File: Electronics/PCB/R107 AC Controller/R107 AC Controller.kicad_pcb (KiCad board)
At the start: 2 copper layers, 56 parts, among them J1 CAR POWER, J2 CONTROL, J3 ACCESSORY, J4 KNOB, J5 THERMOCOUPLE, J6 USB_B_Mini, J7 ISP, K1 G5LE-1, K2 G5LE-1, Q1 MMBT2222ALT1G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

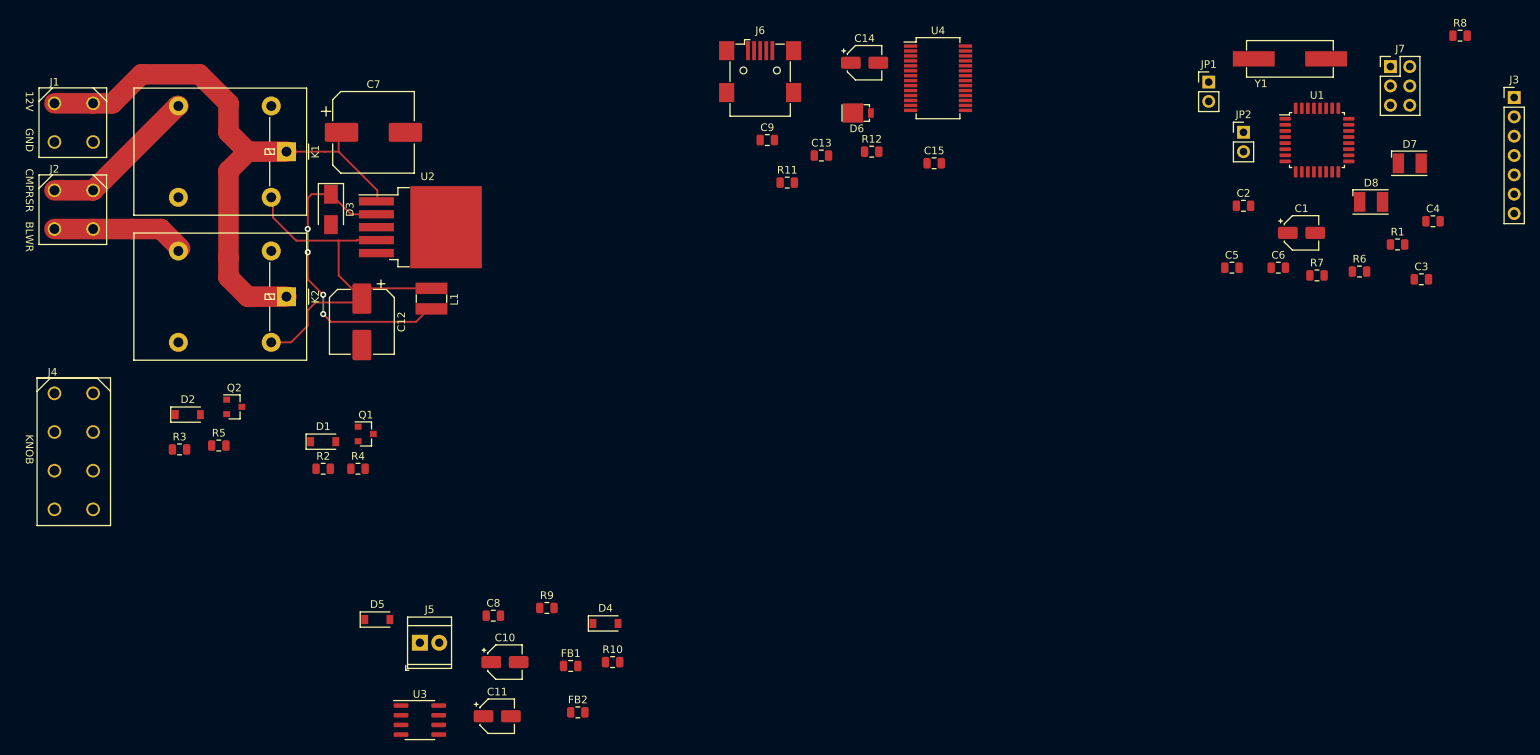
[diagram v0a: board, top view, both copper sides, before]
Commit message: Working on PCB. Added status LED and removed comms LEDs. Added jumper to reduce chances of noise on RX input keeping bootloader running.
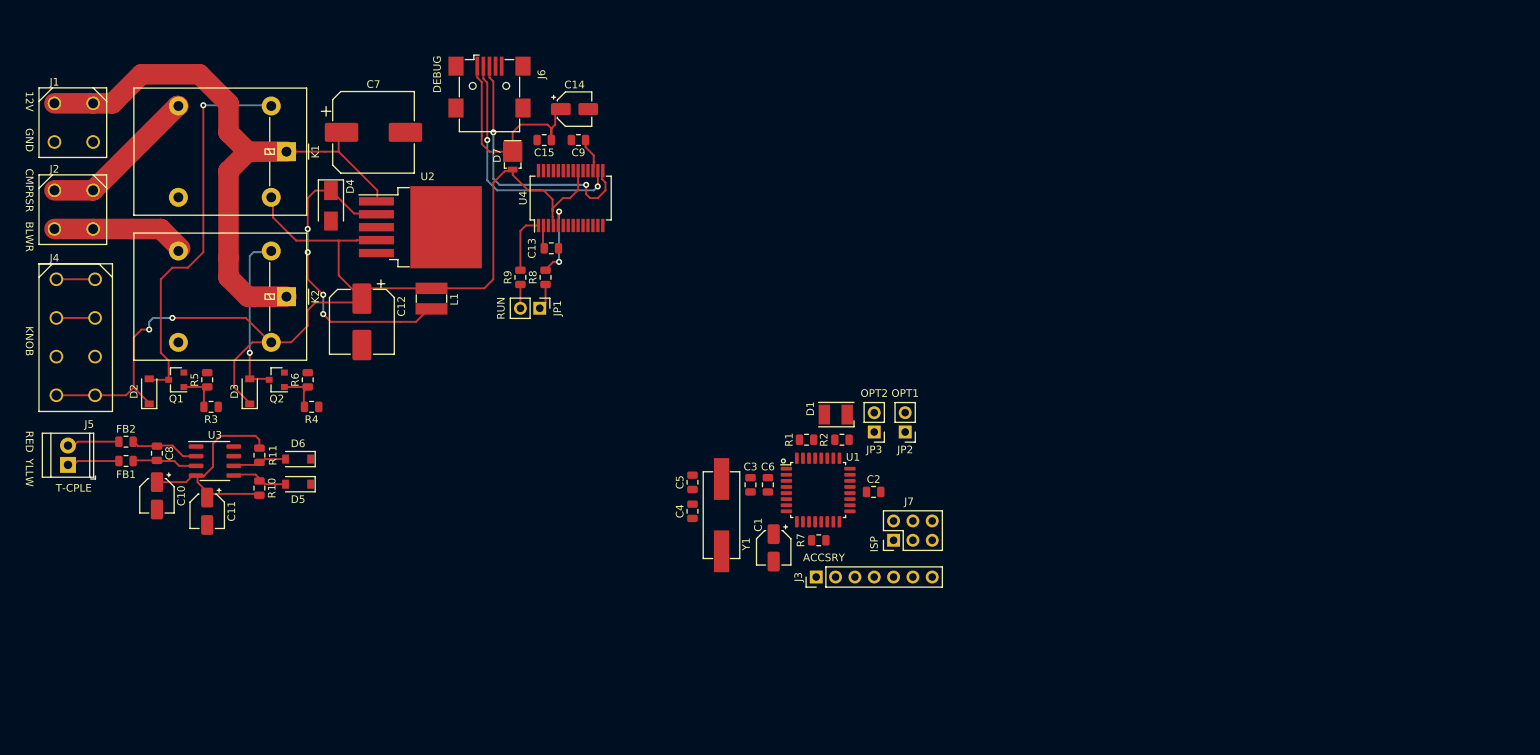
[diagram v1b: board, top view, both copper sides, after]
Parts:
- removed D8: GRN, LED_SMD:LED_PLCC-2
- removed R12: 1K, Resistor_SMD:R_0805_2012Metric
- added JP3: OPT2, Connector_PinHeader_2.54mm:PinHeader_1x02_P2.54mm_Vertical, F.Cu at (241.0, 69.8)
- D1: value MMSD4148T1G -> RED; footprint Diode_SMD:D_SOD-123 -> LED_SMD:LED_PLCC-2
- D3: value SK34ATR -> MMSD4148T1G; footprint Diode_SMD:D_SMA -> Diode_SMD:D_SOD-123
- D4: value MMSD4148T1G -> SK34ATR; footprint Diode_SMD:D_SOD-123 -> Diode_SMD:D_SMA
- D6: value SS1P3L-M3/84A -> MMSD4148T1G; footprint Britishideas:SMP_DO-220AA -> Diode_SMD:D_SOD-123
- D7: value RED -> SS1P3L-M3/84A; footprint LED_SMD:LED_PLCC-2 -> Britishideas:SMP_DO-220AA
- JP1: value OPT1 -> RUN
- JP2: value OPT2 -> OPT1
- R11, R6: value 1K -> 10K
- R4, R9: value 10K -> 1K
- moved R6 138.9 mm to (166.6, 63.0), turned to 90 degrees
- moved R8 124.3 mm to (197.9, 49.5), turned to 90 degrees
- moved D7 117.9 mm to (193.5, 35.4), turned to 270 degrees
- moved J3 111.2 mm to (233.4, 88.9), turned to 90 degrees
- moved C4 104.5 mm to (217.2, 80.3), turned to 90 degrees
- moved Y1 95.8 mm to (221.0, 80.8), turned to 90 degrees
- moved JP1 92.8 mm to (197.1, 53.6), turned to 270 degrees
- moved C3 92.2 mm to (224.8, 76.8), turned to 270 degrees
- moved J7 90.2 mm to (243.6, 84.1), turned to 90 degrees
- moved D6 87.9 mm to (165.4, 73.4), turned to 180 degrees
- moved R1 81.8 mm to (232.2, 70.9)
- moved C1 80.8 mm to (227.8, 85.1), turned to 270 degrees
- moved U1 80.1 mm to (233.7, 77.5)
- moved R11 78.0 mm to (160.3, 72.9), turned to 90 degrees
- moved C5 76.3 mm to (217.2, 76.5), turned to 90 degrees
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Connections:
- D1 pad 1: +5V -> Net-(D1-Pad1)
- D1 pad 2: Net-(D1-Pad2) -> +5V
- D3 pad 1: Net-(D3-Pad1) -> +5V
- D3 pad 2: GND -> Net-(D3-Pad2)
- D4 pad 1: /SCK -> Net-(D4-Pad1)
- D4 pad 2: Net-(D4-Pad2) -> GND
- D5 pad 1: /TC_CS -> /SCK
- D6 pad 1: +5V -> /TC_CS
- D6 pad 2: VBUS -> Net-(D6-Pad2)
- D7 pad 1: Net-(D7-Pad1) -> +5V
- D7 pad 2: +5V -> VBUS
- JP1 pad 2: GND -> Net-(JP1-Pad2)
- K1 pad 2: Net-(D1-Pad2) -> Net-(D2-Pad2)
- K2 pad 2: Net-(D2-Pad2) -> Net-(D3-Pad2)
- L1 pad 1: Net-(D3-Pad1) -> Net-(D4-Pad1)
- Q1 pad 3: Net-(D1-Pad2) -> Net-(D2-Pad2)
- Q2 pad 3: Net-(D2-Pad2) -> Net-(D3-Pad2)
- R11 pad 1: Net-(D7-Pad1) -> Net-(D6-Pad2)
- R11 pad 2: Net-(R11-Pad2) -> +3V3
- R2 pad 1: /COMPRESSOR_CTRL -> Net-(D1-Pad1)
- R2 pad 2: Net-(Q1-Pad1) -> /STATUS
- R3 pad 1: /BLOWER_CTRL -> /COMPRESSOR_CTRL
- R3 pad 2: Net-(Q2-Pad1) -> Net-(Q1-Pad1)
- R4 pad 1: Net-(Q1-Pad1) -> /BLOWER_CTRL
- R4 pad 2: GND -> Net-(Q2-Pad1)
- R5 pad 1: Net-(Q2-Pad1) -> Net-(Q1-Pad1)
- R6 pad 1: Net-(R6-Pad1) -> Net-(Q2-Pad1)
- R6 pad 2: /TX -> GND
- R7 pad 1: Net-(R7-Pad1) -> +5V
- R7 pad 2: /RX -> Net-(R7-Pad2)
- R8 pad 1: +5V -> Net-(JP1-Pad1)
- R8 pad 2: Net-(R8-Pad2) -> /TX
- R9 pad 1: Net-(D4-Pad2) -> Net-(JP1-Pad2)
- R9 pad 2: +3V3 -> /RX
- U1 pad 14: Net-(R8-Pad2) -> Net-(R7-Pad2)
- U1 pad 26: Net-(U1-Pad26) -> /STATUS
- U1 pad 27: Net-(JP1-Pad1) -> Net-(JP2-Pad1)
- U1 pad 28: Net-(JP2-Pad1) -> Net-(JP3-Pad1)
- U1 pad 30: Net-(R7-Pad1) -> Net-(JP1-Pad2)
- U1 pad 31: Net-(R6-Pad1) -> Net-(JP1-Pad1)
- U2 pad 2: Net-(D3-Pad1) -> Net-(D4-Pad1)
- U3 pad 5: Net-(D4-Pad2) -> Net-(D5-Pad2)
- U3 pad 6: Net-(D5-Pad2) -> Net-(D6-Pad2)
- U4 pad 23: Net-(R11-Pad2) -> Net-(U4-Pad23)
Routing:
- net +5V: track 49.8 -> 146.1 mm, vias 0 -> 2
- net Net-(D2-Pad2): track 0.00 -> 51.7 mm, vias 0 -> 1
- net Net-(D3-Pad1): track 41.0 -> 0.00 mm, vias 4 -> 0
- net Net-(D4-Pad1): track 0.00 -> 39.6 mm, vias 0 -> 4
- net Net-(J6-Pad3): track 0.00 -> 34.7 mm, vias 0 -> 2
- net Net-(J6-Pad2): track 0.00 -> 32.6 mm, vias 0 -> 2
- net +3V3: track 0.00 -> 32.3 mm
- net VBUS: track 0.00 -> 28.5 mm
- net Net-(D3-Pad2): track 0.00 -> 21.5 mm, vias 0 -> 1
- net /TX: track 0.00 -> 10.7 mm, vias 0 -> 2
- net Net-(C8-Pad1): track 0.00 -> 9.01 mm
- net Net-(C8-Pad2): track 0.00 -> 8.23 mm
- net /RX: track 0.00 -> 7.76 mm
- net Net-(D5-Pad2): track 0.00 -> 7.00 mm
- net Net-(D6-Pad2): track 0.00 -> 6.54 mm
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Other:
- board text added: "ACCSRY"
- board text added: "DEBUG"
- board text added: "ISP"
- board text added: "OPT1"
- board text added: "OPT2"
- board text added: "RED"
- board text added: "RUN"
- board text added: "T-CPLE"
- board text added: "YLLW"

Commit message: First attempt at PCB.
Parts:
- moved JP2 46.4 mm to (199.4, 61.7)
- moved C1 46.4 mm to (182.1, 76.9)
- moved C2 46.4 mm to (195.2, 69.6)
- moved C3 46.4 mm to (179.1, 68.7)
- moved C4 46.4 mm to (171.4, 72.1)
- moved C5 46.4 mm to (171.4, 68.3)
- moved C6 46.4 mm to (181.4, 68.7)
- moved D1 46.4 mm to (190.3, 59.4)
- moved J3 46.4 mm to (187.7, 80.8)
- moved J7 46.4 mm to (197.9, 75.9)
- moved JP3 46.4 mm to (195.3, 61.7)
- moved R1 46.4 mm to (186.4, 62.7)
- moved R2 46.4 mm to (191.1, 62.7)
- moved R7 46.4 mm to (188.0, 75.9)
- moved U1 46.4 mm to (188.0, 69.3)
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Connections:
- J3 pad 2: /BLOWER_CTRL -> /COMPRESSOR_CTRL
- J3 pad 3: /COMPRESSOR_CTRL -> /ON_OFF
- J3 pad 4: /TEMP_SETTING -> /BLOWER_CTRL
- J3 pad 5: /ON_OFF -> /TEMP_SETTING
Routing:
- net /ON_OFF: track 5.08 -> 102.6 mm, vias 0 -> 6
- net /TEMP_SETTING: track 5.08 -> 94.2 mm, vias 0 -> 11
- net +3V3: track 32.3 -> 97.0 mm, vias 0 -> 2
- net +5V: track 146.1 -> 209.8 mm, vias 2 -> 4
- net /COMPRESSOR_CTRL: track 0.00 -> 61.6 mm, vias 0 -> 4
- net /MISO: track 0.00 -> 60.4 mm, vias 0 -> 3
- net GND: track 0.00 -> 57.3 mm, vias 0 -> 16
- net /RESET: track 0.00 -> 52.7 mm, vias 0 -> 2
- net /SCK: track 0.00 -> 46.3 mm, vias 0 -> 3
- net /BLOWER_CTRL: track 0.00 -> 39.6 mm, vias 0 -> 5
- net /ACC_IO: track 0.00 -> 27.3 mm, vias 0 -> 2
- net /TC_CS: track 0.00 -> 27.3 mm, vias 0 -> 2
- net Net-(JP1-Pad1): track 3.44 -> 30.4 mm, vias 0 -> 4
- net Net-(JP1-Pad2): track 2.87 -> 24.6 mm, vias 0 -> 2
- net Net-(C4-Pad1): track 0.00 -> 17.5 mm, vias 0 -> 2
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- added copper zone on B.Cu, net GND
- added copper zone on F.Cu, net GND
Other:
- board outline added: 80 x 66 mm
- board text added: "R107/C107 AC CONTROLLER REV 1 (C) ANDY@BRITISHIDEAS.COM 2021"

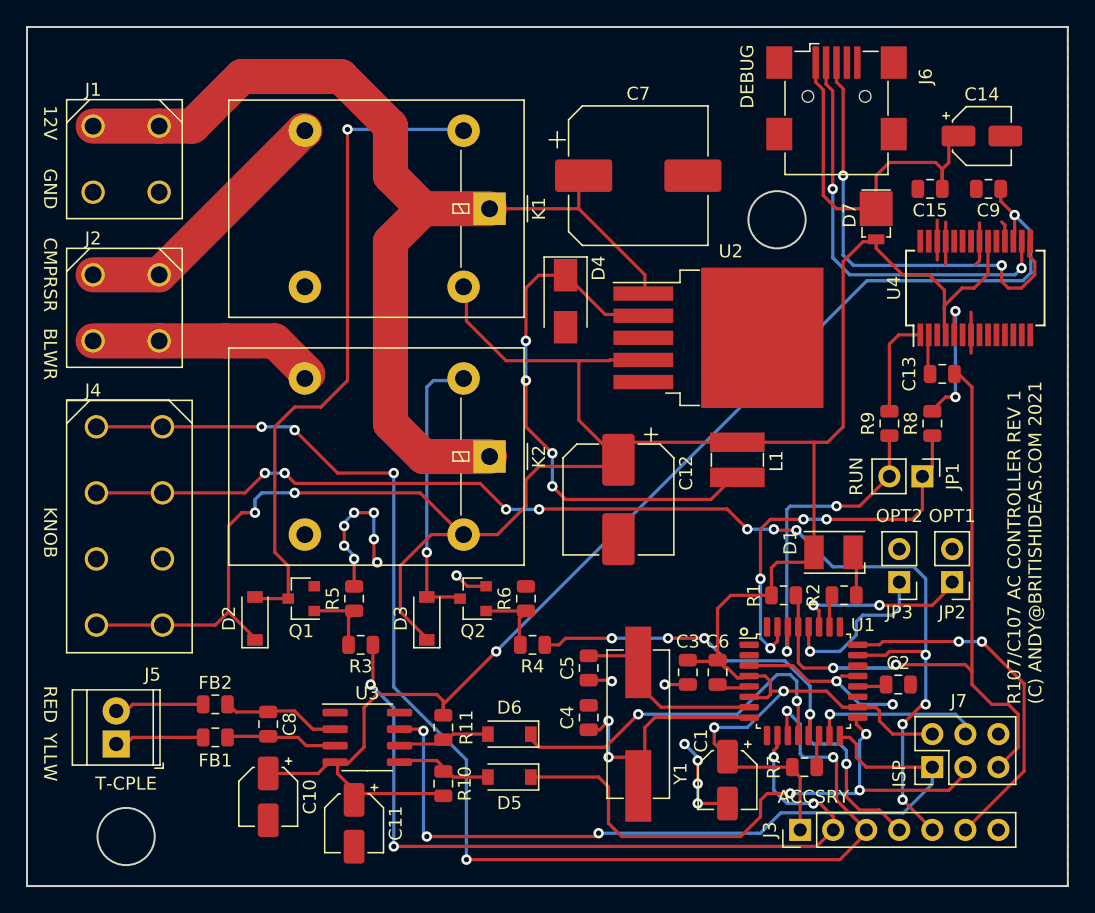
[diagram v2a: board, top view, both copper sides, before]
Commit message: Working on PCB. Adding 3D models. Moved silkscreen text away from vias where possible.
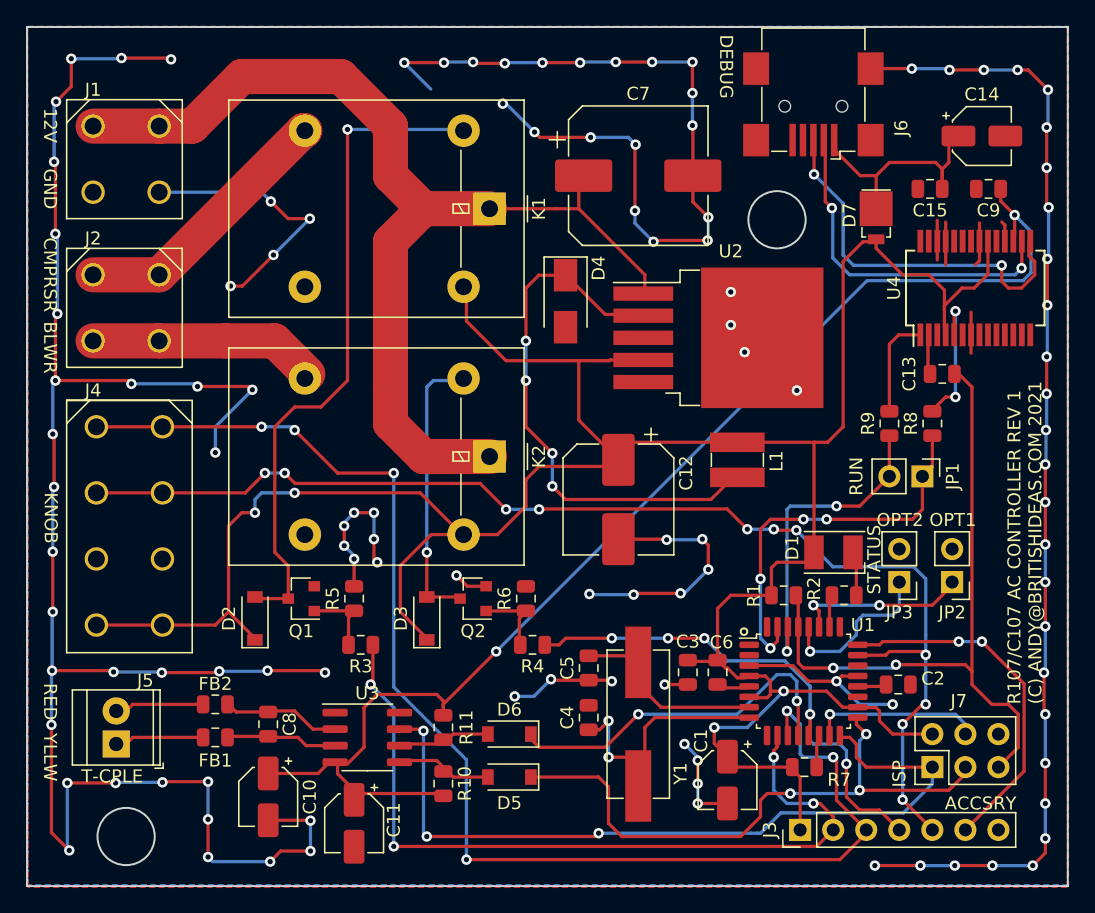
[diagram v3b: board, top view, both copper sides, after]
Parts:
- moved J6 1.93 mm to (188.7, 25.1), turned to 180 degrees
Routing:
- net GND: track 57.3 -> 416.5 mm, vias 16 -> 112
- net VBUS: track 28.5 -> 17.4 mm
- net Net-(J6-Pad2): track 32.6 -> 25.9 mm
- net Net-(J6-Pad3): track 34.7 -> 28.9 mm
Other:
- board text added: "STATUS"

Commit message: Completed 3D models. Fixed mistake with footprint for L1 - was too small.
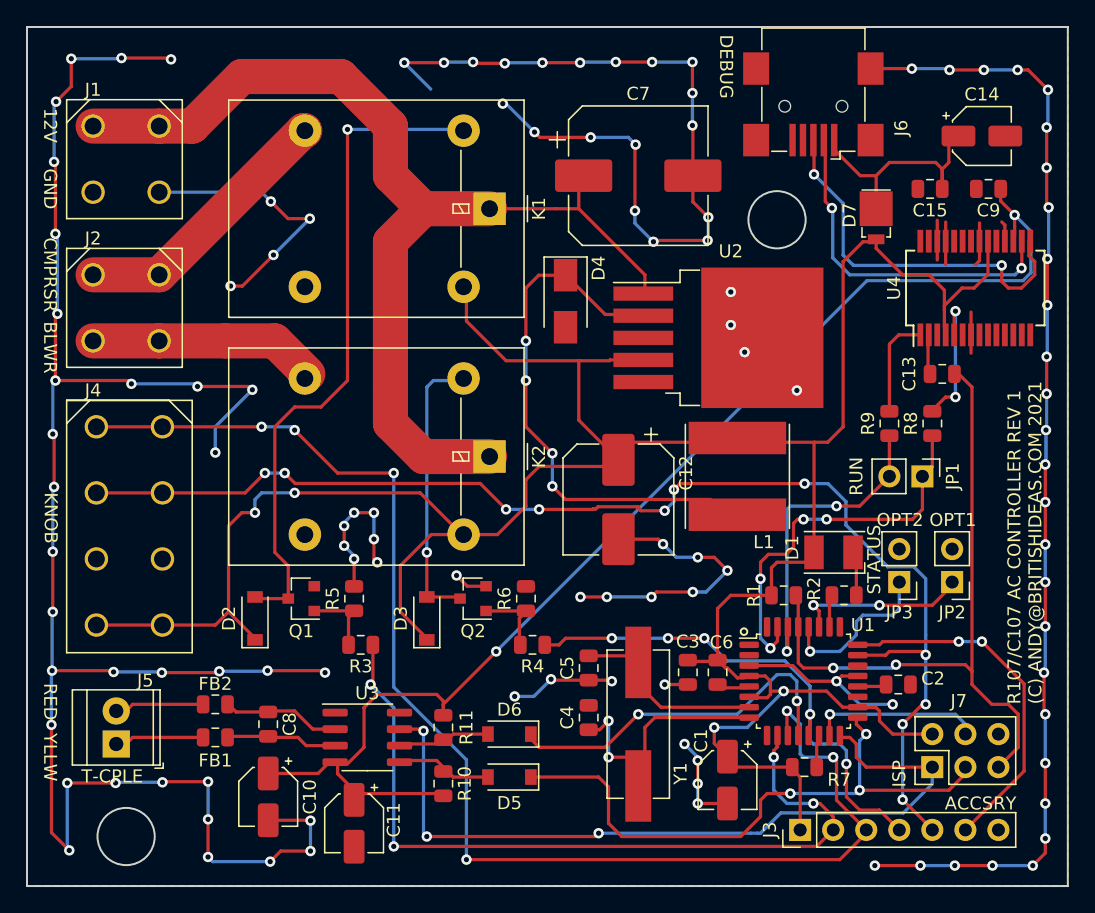
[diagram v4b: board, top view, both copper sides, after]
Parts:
- L1: footprint Britishideas:Chilisin_Power_Inductor_AWVS -> Britishideas:Chilisin_Power_Inductor_AWVS_808040
- moved L1 1.27 mm to (182.9, 53.6)
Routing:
- net /TEMP_SETTING: track 94.2 -> 97.9 mm
- net GND: track 416.5 -> 419.0 mm, vias 112 -> 113
- net Net-(D4-Pad1): track 39.6 -> 37.5 mm
